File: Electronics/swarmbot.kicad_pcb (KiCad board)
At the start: 2 copper layers, 100 x 180 mm, 107 parts, among them J1 8P8C, J2 12x2 JST, J3 12x2 JST, J4 Conn_01x04_Male, J5 Battery 1S2P, J6 Raspberry_Pi_2_3, Q1 BSH108, Q2 BSH108, Q3 BSH108, Q4 BSH108, Q5 RSC002P03, Q6 RSC002P03, SW1 Left, SW2 Right, SW3 SW_SPST, U1 MPC17531A, U10 TP4056, U12 AP9101CK, U13 AP2112K-3.3, U14 INA138, U4 QRE1113GR, U5 QRE1113GR, U6 QRE1113GR, U7 QRE1113GR, U8 QRE1113GR, U9 ESP32-WROOM-32D

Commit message: del backups
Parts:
- moved R32 3.01 mm to (136.3, 172.9), turned to 90 degrees
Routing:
- net /Top PCB/Power/PowerInInrush: track 48.2 -> 49.4 mm, vias 1 -> 2
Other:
- board text added: "When re-importing changes to the PCB from the DXF file, the location is X 120 Y 50, and X 120 Y 150 on the layer Edge.Cuts. You will then need to un-group the imported pcb, and move some features to F.Fab (center lines etc)"
- board text removed: "When re-importing changes to the PCB from the DXF file, the location is X 120 Y 50, and X 120 Y 150 on the layer Edge.Cuts. You will then need to un-group the imported pcb, and move some features to User.1 (center lines etc)"
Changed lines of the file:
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@@
   )
   (footprint "Resistor_SMD:R_0805_2012Metric_Pad1.20x1.40mm_HandSolder" (layer "F.Cu")
-    (at 136.2202 169.8912 -90)
+    (at 136.3 172.9 90)
     (descr "Resistor SMD 0805 (2012 Metric), square (rectangular) end terminal, IPC_7351 nominal with elongated pad for handsoldering. (Body size source: IPC-SM-782 page 72, https://www.pcb-3d.com/wordpress/wp-content/uploads/ipc-sm-782a_amendment_1_and_2.pdf), generated with kicad-footprint-generator")
     (tags "resistor handsolder")
@@
     (fp_line (start 1 0.625) (end -1 0.625) (layer "F.Fab") (width 0.1))
     (fp_line (start 1 -0.625) (end 1 0.625) (layer "F.Fab") (width 0.1))
-    (pad "1" smd roundrect locked (at -1 0 270) (size 1.2 1.4) (layers "F.Cu" "F.Paste" "F.Mask") (roundrect_rratio 0.208333)
+    (pad "1" smd roundrect locked (at -1 0 90) (size 1.2 1.4) (layers "F.Cu" "F.Paste" "F.Mask") (roundrect_rratio 0.208333)
       (net 1 "GND") (pintype "passive"))
-    (pad "2" smd roundrect locked (at 1 0 270) (size 1.2 1.4) (layers "F.Cu" "F.Paste" "F.Mask") (roundrect_rratio 0.208333)
+    (pad "2" smd roundrect locked (at 1 0 90) (size 1.2 1.4) (layers "F.Cu" "F.Paste" "F.Mask") (roundrect_rratio 0.208333)
       (net 117 "Net-(R32-Pad2)") (pintype "passive"))
     (model "${KICAD6_3DMODEL_DIR}/Resistor_SMD.3dshapes/R_0805_2012Metric.wrl"
@@
   (gr_line locked (start 120 157.5) (end 120 142.5) (layer "F.Fab") (width 0.2))
   (gr_line locked (start 112.5 150) (end 127.5 150) (layer "F.Fab") (width 0.2))
-  (gr_text "JLCJLCJLCJLC" (at 261.112 71.12 -90) (layer "B.SilkS")
+  (gr_text "JLCJLCJLCJLC" (at 207.85 71.8 -90) (layer "B.SilkS")
     (effects (font (size 1.5 1.5) (thickness 0.3)) (justify mirror))
   )
@@
     (effects (font (size 1.5 1.5) (thickness 0.3)))
   )
-  (gr_text "When re-importing changes to the PCB from the DXF file, the location is X 120 Y 50, and \nX 120 Y 150 on the layer Edge.Cuts.\n\nYou will then need to un-group the imported pcb, and move some features to User.1 (center \nlines etc)\n" (at 185.928 178.054) (layer "Cmts.User")
+  (gr_text "When re-importing changes to the PCB from the DXF file, the location is X 120 Y 50, and \nX 120 Y 150 on the layer Edge.Cuts.\n\nYou will then need to un-group the imported pcb, and move some features to F.Fab (center \nlines etc)\n" (at 185.928 178.054) (layer "Cmts.User")
     (effects (font (size 1 1) (thickness 0.15)) (justify left))
   )
-  (via (at 129.25 121) (size 0.8) (drill 0.4) (layers "F.Cu" "B.Cu") (free) (net 1))
-  (via (at 126.25 120.25) (size 0.8) (drill 0.4) (layers "F.Cu" "B.Cu") (free) (net 1))
-  (via (at 124.25 118.449509) (size 0.8) (drill 0.4) (layers "F.Cu" "B.Cu") (free) (net 1))
+  (via (at 128.8 118.75) (size 0.8) (drill 0.4) (layers "F.Cu" "B.Cu") (free) (net 1))
+  (via (at 127.6 118.75) (size 0.8) (drill 0.4) (layers "F.Cu" "B.Cu") (free) (net 1))
+  (via (at 124 118.7) (size 0.8) (drill 0.4) (layers "F.Cu" "B.Cu") (free) (net 1))
   (via (at 131.826 116) (size 0.8) (drill 0.4) (layers "F.Cu" "B.Cu") (net 1))
   (via (at 131 118.75) (size 0.8) (drill 0.4) (layers "F.Cu" "B.Cu") (free) (net 1))
   (segment (start 131.826 115.131) (end 131.826 116) (width 0.5) (layer "B.Cu") (net 1))
-  (segment (start 131 119.25) (end 131 118.75) (width 0.5) (layer "B.Cu") (net 1))
-  (segment (start 129.25 121) (end 131 119.25) (width 0.5) (layer "B.Cu") (net 1))
-  (segment (start 124.449509 118.449509) (end 126.25 120.25) (width 0.5) (layer "B.Cu") (net 1))
+  (segment (start 124 118.7) (end 124.05 118.75) (width 0.5) (layer "B.Cu") (net 1))
+  (segment (start 124.05 118.75) (end 127.6 118.75) (width 0.5) (layer "B.Cu") (net 1))
   (segment (start 131.73 115.035) (end 131.826 115.131) (width 0.5) (layer "B.Cu") (net 1))
-  (segment (start 124.25 118.449509) (end 124.449509 118.449509) (width 0.5) (layer "B.Cu") (net 1))
+  (segment (start 128.8 118.75) (end 131 118.75) (width 0.5) (layer "B.Cu") (net 1))
   (segment (start 132.5 128) (end 132.5 126.75) (width 0.5) (layer "F.Cu") (net 2))
   (segment (start 104.149 118.788) (end 101.0334 118.788) (width 0.5) (layer "F.Cu") (net 2))
@@
   (segment (start 161.2486 165.0238) (end 162.109844 165.0238) (width 0.25) (layer "F.Cu") (net 42))
   (segment (start 162.109844 165.0238) (end 164.089029 167.002985) (width 0.25) (layer "F.Cu") (net 42))
+  (segment (start 140.1318 173.4722) (end 140.1474 173.4566) (width 0.5) (layer "F.Cu") (net 43))
   (segment (start 148.463 168.3512) (end 149.6863 168.3512) (width 0.5) (layer "F.Cu") (net 43))
   (segment (start 162.7378 161.8074) (end 166.005 161.8074) (width 0.5) (layer "F.Cu") (net 43))
@@
   (segment (start 164.692414 168.166469) (end 162.833531 168.166469) (width 0.5) (layer "F.Cu") (net 43))
   (segment (start 148.463 169.631) (end 148.4474 169.6466) (width 0.5) (layer "F.Cu") (net 43))
+  (segment (start 140.1318 174.6504) (end 140.1318 173.4722) (width 0.5) (layer "F.Cu") (net 43))
   (via (at 148.463 168.3512) (size 0.8) (drill 0.4) (layers "F.Cu" "B.Cu") (net 43))
+  (via (at 140.1318 174.6504) (size 0.8) (drill 0.4) (layers "F.Cu" "B.Cu") (net 43))
   (segment (start 140.1318 171.468178) (end 143.248778 168.3512) (width 0.5) (layer "B.Cu") (net 43))
   (segment (start 140.1318 174.6504) (end 140.1318 171.468178) (width 0.5) (layer "B.Cu") (net 43))
@@
   (segment (start 157.5214 168.3766) (end 157.5214 166.0214) (width 0.25) (layer "F.Cu") (net 115))
   (segment (start 156.97332 165.47332) (end 154.912398 165.47332) (width 0.25) (layer "F.Cu") (net 115))
-  (segment (start 140.1474 170.9166) (end 136.2456 170.9166) (width 0.25) (layer "F.Cu") (net 117))
-  (segment (start 136.2456 170.9166) (end 136.2202 170.8912) (width 0.25) (layer "F.Cu") (net 117))
+  (segment (start 137.2834 170.9166) (end 136.3 171.9) (width 0.25) (layer "F.Cu") (net 117))
+  (segment (start 136.3 171.9) (end 136.2202 171.8202) (width 0.25) (layer "F.Cu") (net 117))
+  (segment (start 140.1474 170.9166) (end 137.2834 170.9166) (width 0.25) (layer "F.Cu") (net 117))
   (segment (start 153.65 145.2525) (end 154.92 146.5225) (width 0.5) (layer "F.Cu") (net 125))
   (segment (start 151.724 160.5788) (end 151.724 160.569) (width 0.5) (layer "F.Cu") (net 125))

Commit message: yep
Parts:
- added C25: 100nF, Capacitor_SMD:C_0805_2012Metric_Pad1.18x1.45mm_HandSolder, F.Cu at (31.6, 176.9)
- moved L1 100.1 mm to (127.2, 170.9), turned to 180 degrees
- moved C18 35.6 mm to (59.0, 174.3), turned to 90 degrees
- moved C20 33.6 mm to (44.9, 168.2)
- moved U12 25.0 mm to (148.1, 161.1), turned to -90 degrees
- moved R35 21.0 mm to (143.7, 161.1), turned to -90 degrees
- moved C19 11.9 mm to (144.7, 165.8), turned to 0 degrees
- moved U5 0.26 mm to (77.4, 37.9)
- renumbered C17 to C16, C16 to C17, C26 to C23, C23 to C24, C24 to C26, C25 to C27, C27 to C28, C28 to C29, R37 to R35, R38 to R36, R35 to R37, R36 to R38, U14 to U12, U12 to U14
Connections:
- R38 pad 2: +BATT -> /Top PCB/Power/Bat+VE
- U12 pad 3: +BATT -> /Top PCB/Power/Bat+VE
- U12 pad 4: /Top PCB/Power/Bat+VE -> +BATT
- U14 pad 3: unconnected-(U12-Pad3) -> Net-(J5-Pad3)
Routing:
- net +BATT: track 4.11 -> 70.0 mm, vias 0 -> 4
- net /Top PCB/Power/Bat+VE: track 0.00 -> 19.7 mm
- net /Top PCB/ESP32/TX: track 58.6 -> 59.5 mm
- net /Top PCB/ESP32/Bat V: track 29.9 -> 29.2 mm

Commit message: some changes were made
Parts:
- removed the C10 at (86.5, 121.5)
- removed ESP1: ESP Programming TagConnect, TC2030-IDC:Tag-Connect_TC2030-IDC-NL_2x03_P1.27mm_Vertical
- added C7: 10uF, Capacitor_SMD:C_0805_2012Metric_Pad1.18x1.45mm_HandSolder, B.Cu at (103.8, 52.8)
- added D10: Power, LED_SMD:LED_0805_2012Metric_Pad1.15x1.40mm_HandSolder, B.Cu at (115.3, 102.9)
- added D11: SS54, Diode_SMD:D_SMC_Handsoldering, F.Cu at (123.4, 176.3)
- added D12: RBR3LAM30BTFTR, Diode_SMD:D_SOD-128, F.Cu at (123.4, 170.4)
- added D8: Charging, LED_SMD:LED_0805_2012Metric_Pad1.15x1.40mm_HandSolder, B.Cu at (124.5, 102.8)
- added D9: Standby, LED_SMD:LED_0805_2012Metric_Pad1.15x1.40mm_HandSolder, B.Cu at (120.0, 102.8)
- added Front1: Front, Connector_JST:JST_XH_B2B-XH-A_1x02_P2.50mm_Vertical, F.Cu at (107.5, 108.3)
- added Q10: RSC002P03, Package_TO_SOT_SMD:SOT-23, F.Cu at (122.4, 135.9)
- added Q7: BSH108, Package_TO_SOT_SMD:SOT-23, F.Cu at (112.5, 148.6)
- added Q8: BSH108, Package_TO_SOT_SMD:SOT-23, F.Cu at (116.8, 148.6)
- added Q9: BSH108, Package_TO_SOT_SMD:SOT-23, F.Cu at (117.9, 135.9)
- added R39: 1k, Resistor_SMD:R_0805_2012Metric_Pad1.20x1.40mm_HandSolder, F.Cu at (125.0, 113.5)
- added R40: 1k, Resistor_SMD:R_0805_2012Metric_Pad1.20x1.40mm_HandSolder, F.Cu at (129.7, 113.6)
- added R41: 1k, Resistor_SMD:R_0805_2012Metric_Pad1.20x1.40mm_HandSolder, F.Cu at (106.9, 119.1)
- added R42: 1k2, Resistor_SMD:R_0805_2012Metric_Pad1.20x1.40mm_HandSolder, F.Cu at (137.2, 119.4)
- added R43: 30k, Resistor_SMD:R_0805_2012Metric_Pad1.20x1.40mm_HandSolder, F.Cu at (138.4, 186.4)
- added R44: 10k, Resistor_SMD:R_0805_2012Metric_Pad1.20x1.40mm_HandSolder, F.Cu at (140.5, 115.6)
- added R45: 10k, Resistor_SMD:R_0805_2012Metric_Pad1.20x1.40mm_HandSolder, F.Cu at (140.5, 112.3)
- added R46: 73k, Resistor_SMD:R_0805_2012Metric_Pad1.20x1.40mm_HandSolder, F.Cu at (117.6, 181.9)
- added R47: 10k, Resistor_SMD:R_0805_2012Metric_Pad1.20x1.40mm_HandSolder, F.Cu at (117.6, 186.2)
- added R48: .0025R, Resistor_SMD:R_1206_3216Metric_Pad1.30x1.75mm_HandSolder, F.Cu at (118.9, 118.9)
- added R49: 2k7, Resistor_SMD:R_0805_2012Metric_Pad1.20x1.40mm_HandSolder, F.Cu at (153.2, 123.4)
- added R50: 2k7, Resistor_SMD:R_0805_2012Metric_Pad1.20x1.40mm_HandSolder, F.Cu at (120.4, 126.7)
- added R51: 330, Resistor_SMD:R_0805_2012Metric_Pad1.20x1.40mm_HandSolder, F.Cu at (113.8, 126.7)
- added REF**: KiCad-Logo2_5mm_SilkScreen, Symbol:KiCad-Logo2_5mm_SilkScreen, B.Cu at (160.5, 56.1)
- added REF**: OSHW-Logo2_7.3x6mm_SilkScreen, Symbol:OSHW-Logo2_7.3x6mm_SilkScreen, B.Cu at (153.7, 146.3)
- added REF**: OSHW-Logo2_7.3x6mm_SilkScreen, Symbol:OSHW-Logo2_7.3x6mm_SilkScreen, B.Cu at (161.0, 45.7)
- added REF**: KiCad-Logo2_5mm_SilkScreen, Symbol:KiCad-Logo2_5mm_SilkScreen, B.Cu at (146.8, 149.9)
- added U15: FDC6303N, Package_TO_SOT_SMD:SOT-23-6_Handsoldering, F.Cu at (131.1, 125.5)
- C16: value 10uF -> 22uF
- C18: value 22uF -> 10uF
- C19: value 10uF -> 100nF
- C20: value 100nF -> 10uF
- C8: renamed from C7; moved to B.Cu
- D1, D2: value RBR3LAM30BTFTR -> IR; footprint Diode_SMD:D_SOD-128 -> LED_THT:LED_D5.0mm; moved to B.Cu
- D3: value Power -> IR; footprint LED_SMD:LED_0805_2012Metric_Pad1.15x1.40mm_HandSolder -> LED_THT:LED_D5.0mm; moved to B.Cu
- D4: value Charging -> IR; footprint LED_SMD:LED_0805_2012Metric_Pad1.15x1.40mm_HandSolder -> LED_THT:LED_D5.0mm; moved to B.Cu
- D5: value Standby -> IR; footprint LED_SMD:LED_0805_2012Metric_Pad1.15x1.40mm_HandSolder -> LED_THT:LED_D5.0mm; moved to B.Cu
- D6: value SS54 -> RBR3LAM30BTFTR; footprint Diode_SMD:D_SMC_Handsoldering -> Diode_SMD:D_SOD-128
- J1: value 8P8C -> Top; footprint Connector_RJ:RJ45_Amphenol_54602-x08_Horizontal -> Connector_JST:JST_XH_B2B-XH-A_1x02_P2.50mm_Vertical; moved to B.Cu
- J2, J3: value 12x2 JST -> 12x2 IDC; footprint Connector_JST:JST_PUD_B24B-PUDSS_2x12_P2.00mm_Vertical -> Connector_IDC:IDC-Header_2x12_P2.54mm_Vertical
- Logo1, Logo2, R10, R11, R12, R13, R14, R15, R16, R3, R4, R7, R8, R9, SW3: moved to B.Cu
- Q1: value BSH108 -> AO3400A
- Q2, Q3, Q4: value BSH108 -> Q_Photo_NPN_CE; footprint Package_TO_SOT_SMD:SOT-23 -> LED_THT:LED_D3.0mm_IRBlack
- Q5, Q6: value RSC002P03 -> Q_Photo_NPN_CE; footprint Package_TO_SOT_SMD:SOT-23 -> LED_THT:LED_D3.0mm_IRBlack
- R18: value 10k -> 0Ω
- R19, R20, R21, R22, R23: value 10k -> 470
- R26, R29, R30: value 1k -> 10k
- R27, R28: value 2R -> 10k
- R31: value 30k -> 0Ω
- R32: value 1k2 -> 10k
- R33: value 73k -> 10k
- R35: value .0025R -> 10k; footprint Resistor_SMD:R_1206_3216Metric_Pad1.30x1.75mm_HandSolder -> Resistor_SMD:R_0805_2012Metric_Pad1.20x1.40mm_HandSolder
- R36: value 2k7 -> 10k
- R37: value 2k7 -> 2R
- R38: value 330 -> 2R
- moved R30 137.5 mm to (122.0, 35.8)
- moved R31 136.2 mm to (121.9, 32.5)
- moved C27 124.9 mm to (158.0, 174.2), turned to 90 degrees
- moved U13 122.5 mm to (150.6, 174.2), turned to -90 degrees
- moved C26 114.8 mm to (154.7, 174.2), turned to 90 degrees
- moved C20 113.4 mm to (153.2, 134.6), turned to 180 degrees
- moved Logo1 108.5 mm to (153.4, 153.7), turned to -90 degrees
- moved C24 106.1 mm to (146.6, 174.2), turned to -90 degrees
- moved D7 103.8 mm to (143.3, 120.1), turned to 180 degrees
- moved C25 99.2 mm to (117.1, 126.7), turned to 90 degrees
- moved C17 97.7 mm to (142.2, 174.5)
- moved U14 89.0 mm to (125.5, 125.5)
- moved R18 88.6 mm to (160.5, 165.1), turned to 0 degrees
- moved R17 88.2 mm to (160.5, 162.2)
- moved C21 85.9 mm to (114.0, 181.9), turned to -90 degrees
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- renumbered C9 to C10, C8 to C9
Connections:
- net Net-(J5-Pad3) renamed /Top PCB/Power/bat-ve
- C11 pad 1: /Line Sensor LEDs Top -> /Top PCB/ESP32/5V Switched 1
- C14 pad 1: /Top PCB/ESP32/Bat V -> /Top PCB/Power/PowerInDiode
- C15 pad 1: /Top PCB/Power/PowerInDiode -> /Top PCB/Power/PowerInInrush
- C16 pad 1: /Top PCB/Power/PowerInInrush -> /Top PCB/Power/VBAT
- C18 pad 1: /Top PCB/Power/VBAT -> +BATT
- C20 pad 1: +BATT -> /Top PCB/ESP32/Bat V
- D1 pad 1: /Top PCB/Power/+BatDiode -> Net-(D1-Pad1)
- D1 pad 2: +BATT -> Net-(D1-Pad2)
- D2 pad 1: /Top PCB/Power/PowerInDiode -> Net-(D1-Pad1)
- D2 pad 2: /Top PCB/Power In -> Net-(D2-Pad2)
- D3 pad 1: Net-(D3-Pad1) -> Net-(D1-Pad1)
- D3 pad 2: /Top PCB/Power/VBAT -> Net-(D3-Pad2)
- D4 pad 1: Net-(D4-Pad1) -> Net-(D1-Pad1)
- D4 pad 2: /Top PCB/Power/PowerInInrush -> Net-(D4-Pad2)
- D5 pad 1: Net-(D5-Pad1) -> Net-(D1-Pad1)
- D5 pad 2: /Top PCB/Power/PowerInInrush -> Net-(D5-Pad2)
- D6 pad 1: +5V -> /Top PCB/Power/PowerInDiode
- D6 pad 2: /Top PCB/Power/vbatInductor -> /Top PCB/Power/Power In
- D7 pad 1: +5V -> /Top PCB/Power/+BatDiode
- D7 pad 2: /Top PCB/Power/PowerIn -> +BATT
- J1 pad 1: unconnected-(J1-Pad1) -> /Top PCB/Power/Power In
- J1 pad 2: unconnected-(J1-Pad2) -> GND
- J2 pad 1: /Left Motor Sensor Top -> GND
- J2 pad 10: GND -> /Line Sensor 4 Top
- J2 pad 11: /Sonar Echo Top -> unconnected-(J2-Pad11)
- J2 pad 12: GND -> /Sonar Echo Top
- J2 pad 13: /Sonar Trigger Top -> unconnected-(J2-Pad13)
- J2 pad 14: +5V -> /Sonar Trigger Top
- J2 pad 15: /Line Sensor 3 Top -> unconnected-(J2-Pad15)
- J2 pad 16: +5V -> /Line Sensor 3 Top
- J2 pad 17: /Line Sensor 2 Top -> /Bottom PCB V
- J2 pad 18: +3V3 -> /Line Sensor 2 Top
- J2 pad 19: /Right Switch Top -> GND
- J2 pad 2: /H-Bridge 1B Top -> /Left Motor Sensor Top
- J2 pad 20: unconnected-(J2-Pad20) -> /Right Switch Top
- J2 pad 21: /Line Sensor 1 Top -> +5V
- J2 pad 22: unconnected-(J2-Pad22) -> /Line Sensor 1 Top
- J2 pad 23: /Right Motor Sensor Top -> +3V3
- J2 pad 24: unconnected-(J2-Pad24) -> /Right Motor Sensor Top
- J2 pad 3: /Line Sensor 5 Top -> /H-Bridge 1B Top
- J2 pad 4: /H-Bridge 1A Top -> /Line Sensor 5 Top
- J2 pad 5: /Line Sensor LEDs Top -> /H-Bridge 1A Top
- J2 pad 6: /H-Bridge 2A Top -> /Line Sensor LEDs Top
- J2 pad 7: /Left Switch Top -> /H-Bridge 2A Top
- J2 pad 8: /H-Bridge 2B Top -> /Left Switch Top
- J2 pad 9: /Line Sensor 4 Top -> /H-Bridge 2B Top
- J3 pad 1: /Left Motor Sensor Lower -> /Lower PCB GND
- J3 pad 10: /Lower PCB GND -> /Line Sensor 4 Lower
- J3 pad 11: /Sonar Echo Lower -> /Lower PCB 5V
- J3 pad 12: /Lower PCB GND -> /Sonar Echo Lower
- J3 pad 13: /Sonar Trigger Lower -> unconnected-(J3-Pad13)
- J3 pad 14: /Lower PCB 5V -> /Sonar Trigger Lower
- J3 pad 15: /Line Sensor 3 Lower -> unconnected-(J3-Pad15)
- J3 pad 16: /Lower PCB 5V -> /Line Sensor 3 Lower
- J3 pad 17: /Line Sensor 2 Lower -> /Bottom PCB Version
- J3 pad 18: /Lower PCB 3V3 -> /Line Sensor 2 Lower
- J3 pad 19: /Right Switch Lower -> /Lower PCB GND
- J3 pad 2: /H-Bridge 1B Lower -> /Left Motor Sensor Lower
- J3 pad 20: unconnected-(J3-Pad20) -> /Right Switch Lower
- J3 pad 21: /Line Sensor 1 Lower -> /Lower PCB 5V
- J3 pad 22: unconnected-(J3-Pad22) -> /Line Sensor 1 Lower
- J3 pad 23: /Right Motor Sensor Lower -> /Lower PCB 3V3
- J3 pad 24: unconnected-(J3-Pad24) -> /Right Motor Sensor Lower
- J3 pad 3: /Line Sensor 5 Lower -> /H-Bridge 1B Lower
- J3 pad 4: /H-Bridge 1A Lower -> /Line Sensor 5 Lower
- J3 pad 5: /Line Sensor LEDs Lower -> /H-Bridge 1A Lower
- J3 pad 6: /H-Bridge 2A Lower -> /Line Sensor LEDs Lower
- J3 pad 7: /Left Switch Lower -> /H-Bridge 2A Lower
- J3 pad 8: /H-Bridge 2B Lower -> /Left Switch Lower
- J3 pad 9: /Line Sensor 4 Lower -> /H-Bridge 2B Lower
- J4 pad 1: /Lower PCB/Motors/Motor 2B -> /Lower PCB/Motors/Motor 1B
- J4 pad 2: /Lower PCB/Motors/Motor 2A -> /Lower PCB/Motors/Motor 2B
- J4 pad 3: /Lower PCB/Motors/Motor 1B -> /Lower PCB/Motors/Motor 2A
- J6 pad 11: unconnected-(J6-Pad11) -> /Top PCB/ESP32/Reset
- J6 pad 13: unconnected-(J6-Pad13) -> /Top PCB/ESP32/Flash
- J6 pad 16: /Top PCB/ESP32/Flash -> unconnected-(J6-Pad16)
- J6 pad 18: /Top PCB/ESP32/Reset -> unconnected-(J6-Pad18)
- J6 pad 9: GND -> unconnected-(J6-Pad9)
- PenServo1 pad 3: /Top PCB/ESP32/Pen Servo -> /Top PCB/Pen Servo
- Q1 pad 1: /Top PCB/ESP32/Flash -> Net-(Q1-Pad1)
- Q1 pad 3: /Top PCB/ESP32/program -> Net-(D1-Pad1)
- Q2 pad 1: /Top PCB/ESP32/Reset -> +3V3
- Q2 pad 2: GND -> /Top PCB/ESP32/IR_1
- Q3 pad 1: Net-(Q3-Pad1) -> +3V3
- Q3 pad 2: GND -> /Top PCB/ESP32/IR_2
- Q4 pad 1: Net-(Q4-Pad1) -> +3V3
- Q4 pad 2: GND -> /Top PCB/ESP32/IR_3
- Q5 pad 1: /Top PCB/ESP32/5V Switched 1 -> +3V3
- Q5 pad 2: Net-(Q3-Pad3) -> /Top PCB/ESP32/IR_4
- Q6 pad 1: /Line Sensor LEDs Top -> +3V3
- Q6 pad 2: Net-(Q4-Pad3) -> /Top PCB/ESP32/IR_5
- R1 pad 1: /Lower PCB 5V -> /Lower PCB 3V3
- R17 pad 1: /Top PCB/ESP32/5V Switch Aux -> /Top PCB/ESP32/Top PCB V
- R17 pad 2: Net-(Q3-Pad1) -> +3V3
- R18 pad 1: /Top PCB/ESP32/5V Switch 1 -> GND
- R18 pad 2: Net-(Q3-Pad1) -> /Top PCB/ESP32/Top PCB V
- R19 pad 1: /Top PCB/ESP32/Line Sensor LED -> +3V3
- R19 pad 2: Net-(Q4-Pad1) -> Net-(D1-Pad2)
- R2 pad 1: /Lower PCB 5V -> /Lower PCB 3V3
- R20 pad 2: /Top PCB/ESP32/program -> Net-(D2-Pad2)
- R21 pad 2: /Top PCB/ESP32/enable -> Net-(D3-Pad2)
- R22 pad 1: +5V -> +3V3
- R22 pad 2: Net-(Q3-Pad3) -> Net-(D4-Pad2)
- R23 pad 1: +5V -> +3V3
- R23 pad 2: Net-(Q4-Pad3) -> Net-(D5-Pad2)
- R24 pad 1: /Top PCB/ESP32/Bat V -> /Top PCB/ESP32/IR_LEDS
- R24 pad 2: +BATT -> Net-(Q1-Pad1)
- R25 pad 2: /Top PCB/ESP32/Bat V -> /Top PCB/ESP32/IR_1
- R26 pad 2: Net-(D3-Pad1) -> /Top PCB/ESP32/IR_2
- R27 pad 1: /Top PCB/Power/PowerInInrush -> GND
- R27 pad 2: /Top PCB/Power/PowerInDiode -> /Top PCB/ESP32/IR_3
- R28 pad 1: /Top PCB/Power/PowerInInrush -> GND
- R28 pad 2: /Top PCB/Power/PowerInDiode -> /Top PCB/ESP32/IR_4
- R29 pad 1: Net-(R29-Pad1) -> GND
- R29 pad 2: Net-(D4-Pad1) -> /Top PCB/ESP32/IR_5
- R30 pad 1: Net-(D5-Pad1) -> /Bottom PCB Version
- R30 pad 2: Net-(R30-Pad2) -> /Lower PCB 3V3
- R31 pad 1: GND -> /Lower PCB GND
- R31 pad 2: Net-(R31-Pad2) -> /Bottom PCB Version
- R32 pad 1: GND -> Net-(Q9-Pad1)
- R32 pad 2: Net-(R32-Pad2) -> /Top PCB/ESP32/5V Switch Aux
- R33 pad 1: Net-(R33-Pad1) -> Net-(Q9-Pad1)
- R33 pad 2: +5V -> /Top PCB/ESP32/5V Switch 1
- R34 pad 1: GND -> /Top PCB/ESP32/program
- R34 pad 2: Net-(R33-Pad1) -> +3V3
- R35 pad 1: /Top PCB/Power/Bat+VE -> /Top PCB/ESP32/enable
- R35 pad 2: +BATT -> +3V3
- R36 pad 1: /Top PCB/ESP32/Bat I -> Net-(Q10-Pad2)
- R36 pad 2: Net-(R36-Pad2) -> +5V
- R37 pad 1: GND -> /Top PCB/Power/PowerInInrush
- R37 pad 2: Net-(R37-Pad2) -> /Top PCB/Power/PowerInDiode
- R38 pad 1: Net-(C25-Pad1) -> /Top PCB/Power/PowerInInrush
- R38 pad 2: /Top PCB/Power/Bat+VE -> /Top PCB/Power/PowerInDiode
- U10 pad 2: Net-(R32-Pad2) -> Net-(R42-Pad2)
- U10 pad 6: Net-(R30-Pad2) -> Net-(R40-Pad2)
- U10 pad 7: Net-(R29-Pad1) -> Net-(R39-Pad1)
- U12 pad 1: Net-(R36-Pad2) -> Net-(R49-Pad2)
- U14 pad 1: Net-(R37-Pad2) -> Net-(R50-Pad2)
- U14 pad 4: unconnected-(U14-Pad4) -> Net-(U14-Pad4)
- U14 pad 5: unconnected-(U14-Pad5) -> Net-(U14-Pad5)
- U9 pad 10: unconnected-(U9-Pad10) -> /Top PCB/ESP32/Bat I
- U9 pad 12: unconnected-(U9-Pad12) -> /Top PCB/ESP32/5V Switch 1
- U9 pad 13: unconnected-(U9-Pad13) -> /Left Motor Sensor Top
- U9 pad 14: unconnected-(U9-Pad14) -> /Line Sensor 5 Top
- U9 pad 16: unconnected-(U9-Pad16) -> /Top PCB/ESP32/enable
- U9 pad 18: /H-Bridge 1A Top -> /Line Sensor LEDs Top
- U9 pad 19: /H-Bridge 2A Top -> /H-Bridge 1A Top
- U9 pad 20: /H-Bridge 2B Top -> /Left Switch Top
- U9 pad 21: unconnected-(U9-Pad21) -> /H-Bridge 2A Top
- U9 pad 22: /Left Motor Sensor Top -> /Line Sensor 4 Top
- U9 pad 23: /Line Sensor 5 Top -> /H-Bridge 2B Top
- U9 pad 24: /Left Switch Top -> /Sonar Echo Top
- U9 pad 26: /Line Sensor 4 Top -> /Sonar Trigger Top
- U9 pad 27: /Sonar Echo Top -> /Line Sensor 3 Top
- U9 pad 28: /Sonar Trigger Top -> /Line Sensor 2 Top
- U9 pad 29: /Line Sensor 3 Top -> /Bottom PCB V
- U9 pad 3: /Top PCB/ESP32/enable -> /Top PCB/ESP32/IR_1
- U9 pad 30: /Line Sensor 2 Top -> /Right Switch Top
- U9 pad 31: /Right Switch Top -> /Line Sensor 1 Top
- U9 pad 33: /Line Sensor 1 Top -> /Right Motor Sensor Top
- U9 pad 36: /Right Motor Sensor Top -> /Top PCB/Pen Servo
- U9 pad 37: /Top PCB/ESP32/Line Sensor LED -> /Top PCB/ESP32/Top PCB V
- U9 pad 4: /Top PCB/ESP32/5V Switch 1 -> /Top PCB/ESP32/IR_2
- U9 pad 5: /Top PCB/ESP32/Pen Servo -> /Top PCB/ESP32/IR_3
- U9 pad 6: /Top PCB/ESP32/Bat V -> /Top PCB/ESP32/IR_4
- U9 pad 7: /Top PCB/ESP32/Bat I -> /Top PCB/ESP32/IR_5
- U9 pad 8: unconnected-(U9-Pad8) -> /Top PCB/ESP32/IR_LEDS
- U9 pad 9: unconnected-(U9-Pad9) -> /Top PCB/ESP32/Bat V
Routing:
- net /Top PCB/ESP32/IR_5: track 0.00 -> 173.0 mm
- net /Top PCB/Power/Power In: track 0.00 -> 170.8 mm, vias 0 -> 1
- net /Top PCB/ESP32/IR_4: track 0.00 -> 154.1 mm
- net /Top PCB/ESP32/IR_3: track 0.00 -> 138.0 mm
- net /Top PCB/Power/VBAT: track 6.83 -> 130.6 mm, vias 0 -> 1
- net /Top PCB/ESP32/IR_2: track 0.00 -> 121.0 mm
- net +5V: track 4.79 -> 115.8 mm, vias 4 -> 3
- net /Top PCB/ESP32/IR_1: track 0.00 -> 104.6 mm
- net /Top PCB/ESP32/IR_LEDS: track 0.00 -> 81.9 mm
- net /Top PCB/Pen Servo: track 0.00 -> 80.3 mm, vias 0 -> 1
- net Net-(D1-Pad1): track 0.00 -> 75.3 mm
- net +3V3: track 78.9 -> 15.3 mm, vias 4 -> 13
- net /Top PCB/ESP32/Flash: track 70.7 -> 7.89 mm, vias 1 -> 0
- net Net-(R49-Pad2): track 0.00 -> 59.7 mm
- net /Top PCB/ESP32/Reset: track 68.4 -> 13.3 mm, vias 1 -> 0
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- added copper zone on B.Cu, net +3V3
- added copper zone on F.Cu, net /Lower PCB 3V3
- added copper zone on F.Cu, net /Lower PCB 5V
- added copper zone on B.Cu, net /Lower PCB GND
- removed copper zone on B.Cu, net +5V
- removed copper zone on B.Cu, net /Lower PCB 3V3
- removed copper zone on B.Cu, net /Lower PCB 5V
- removed copper zone on F.Cu, net /Lower PCB GND
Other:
- board size 100 x 180 mm -> 100 x 190 mm
- board text added: "+Ve"
- board text added: "1S2P"
- board text added: "5V DC"
- board text added: "DC 5V Charging"
- board text added: "For Version Information see Schematics"
- board text added: "Swarmbot Bottom PCB Version 1"
- board text added: "Swarmbot Top PCB Version 1"
- board text added: "When re-importing changes to the PCB from the DXF file, the location is X 120 Y 50, and X 120 Y 150. There should be two files, Edge Cuts, and User.2 per pcb."
- board text added: "You lost the game!"
- board text removed: "Swarmbot Lower PCB Version 0.2"
- board text removed: "Swarmbot Top PCB Version 0.2"
- board text removed: "When re-importing changes to the PCB from the DXF file, the location is X 120 Y 50, and X 120 Y 150 on the layer Edge.Cuts. You will then need to un-group the imported pcb, and move some features to F.Fab (center lines etc)"

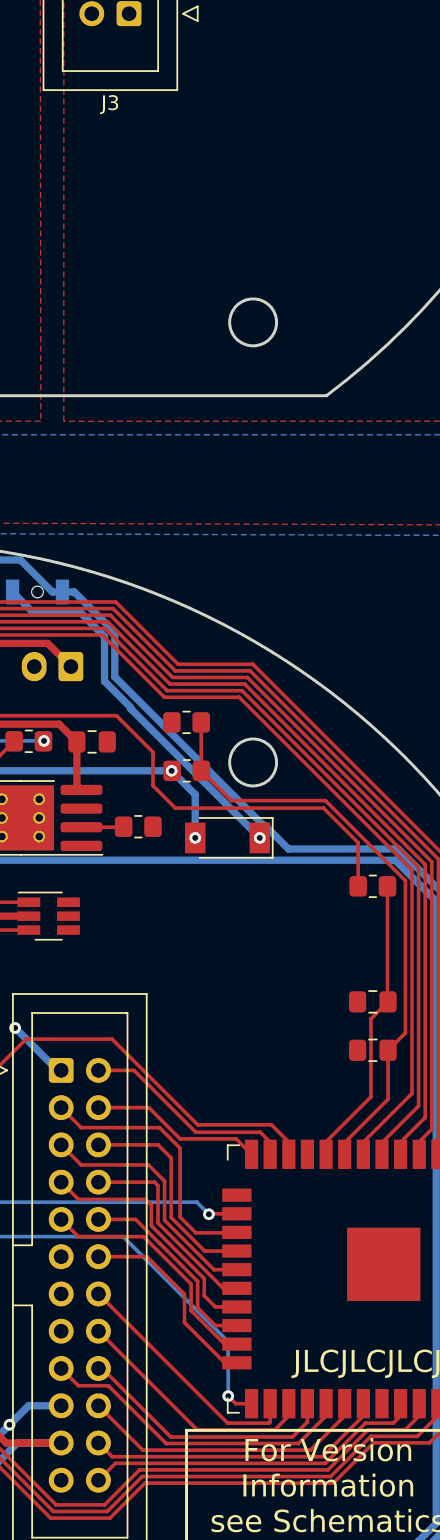
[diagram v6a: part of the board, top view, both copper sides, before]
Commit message: removed the backups
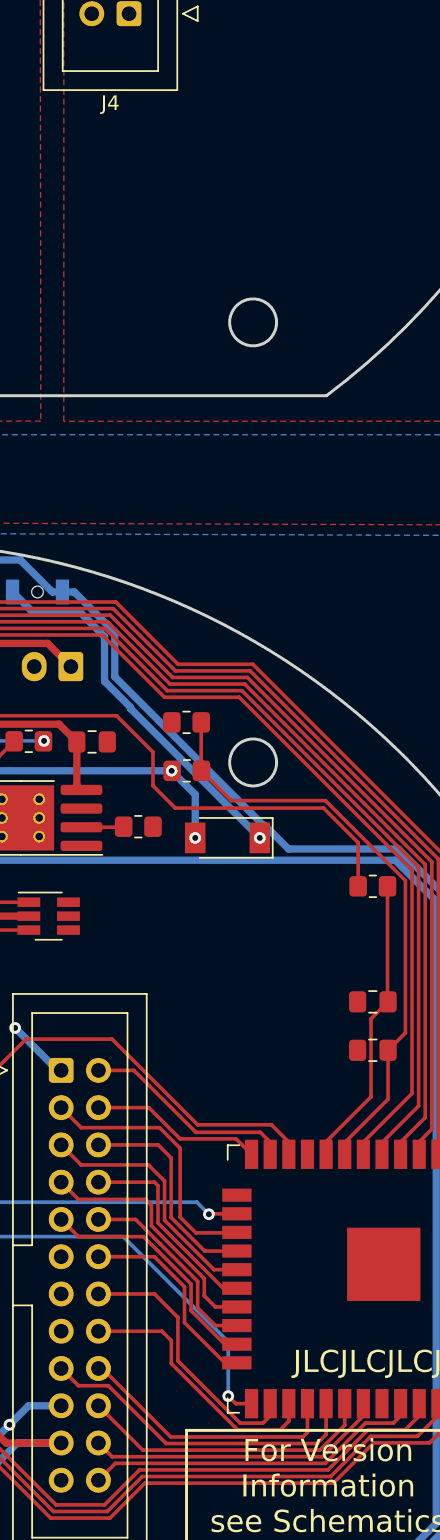
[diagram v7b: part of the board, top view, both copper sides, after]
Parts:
- removed REF** (x2): KiCad-Logo2_5mm_SilkScreen, Symbol:KiCad-Logo2_5mm_SilkScreen
- removed REF** (x2): OSHW-Logo2_7.3x6mm_SilkScreen, Symbol:OSHW-Logo2_7.3x6mm_SilkScreen
- renumbered Front1 to J1, J1 to J2, J2 to J3, J3 to J4, J4 to J5, J5 to J6, J6 to J7
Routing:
- net /Sonar Trigger Top: track 17.3 -> 18.8 mm
- net /Line Sensor 3 Top: track 17.0 -> 18.1 mm
- net /Bottom PCB V: track 21.8 -> 22.5 mm
